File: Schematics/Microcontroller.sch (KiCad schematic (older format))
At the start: 26 parts, among them CON1 USB-MICRO-B, IC1 ATXMEGA256A3BU-A, J1 AVR_JTAG_Header, P1 CONN_02X08, SW1 SW_PUSH, SW2 SW_PUSH, SW3 SW_PUSH, SW4 SW_PUSH, X1 12MHz, X2 32.768KhZ

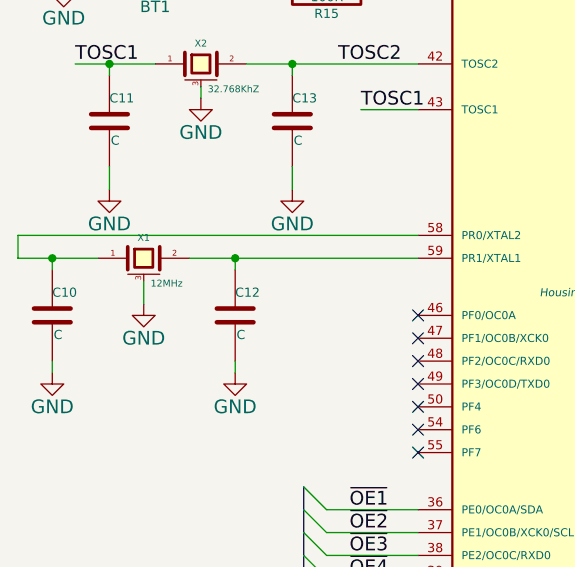
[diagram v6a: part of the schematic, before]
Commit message: Changed lots
Finalised the Inductor. Closes #5
Changed USB Connector. Closes #4
Added four switches for a simple interface. Closes #7
Added a power jack. Closes #3
Found RTC Oscillator. Closes #1.
Added part numbers to all major components. Closes #2
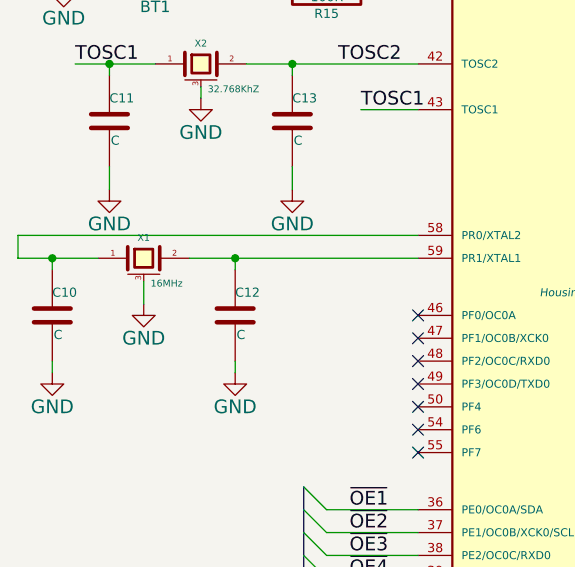
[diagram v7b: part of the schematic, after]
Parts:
- BT1: Part (none) -> BU2032SM-HD-GTR-ND; Supplier (none) -> Digikey
- CON1: footprint usb:USB_Micro-B -> Connect:USB_Mini-B
- IC1: Part (none) -> ATXMEGA256A3BU-A; Supplier (none) -> Farnell
- J1: Part (none) -> FTSH-105-01-L-DV-K-A-P; Supplier (none) -> Farnell
- JP1: footprint SMD_Packages:SMD-0201_r -> Resistors_SMD:R_0603
- P1: footprint (none) -> Socket_Strips:Socket_Strip_Straight_2x08
- SW1, SW2, SW3, SW4: Part (none) -> MC32882; Supplier (none) -> Farnell
- X1: value 12MHz -> 16MHz; Part (none) -> ABM8-16.000MHZ-B2-T; Supplier (none) -> Farnell
- X2: footprint Crystals_Oscillators_SMD:crystal_FA238-TSX3225 -> rgb:SMD_Osc; Part (none) -> ABS06-32.768KHZ-1-T; Supplier (none) -> Farnell
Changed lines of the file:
@@
 F 2 "rgb:FTSH-105-01-L-DV-K-A-P" H 9350 3150 60  0001 C CNN
 F 3 "" H 9350 3150 60  0000 C CNN
+F 4 "FTSH-105-01-L-DV-K-A-P" H 9350 3150 60  0001 C CNN "Part"
+F 5 "Farnell" H 9350 3150 60  0001 C CNN "Supplier"
 	1    9350 3150
 	1    0    0    -1
@@
 SCL
 $Comp
-L VPP #PWR14
+L VPP #PWR03
 U 1 1 54B121F9
 P 9250 1200
-F 0 "#PWR14" H 9250 1050 60  0001 C CNN
+F 0 "#PWR03" H 9250 1050 60  0001 C CNN
 F 1 "VPP" H 9250 1350 60  0000 C CNN
 F 2 "" H 9250 1200 60  0000 C CNN
@@
 $EndComp
 $Comp
-L VPP #PWR10
+L VPP #PWR04
 U 1 1 54B1220F
 P 5800 1450
-F 0 "#PWR10" H 5800 1300 60  0001 C CNN
+F 0 "#PWR04" H 5800 1300 60  0001 C CNN
 F 1 "VPP" H 5800 1600 60  0000 C CNN
 F 2 "" H 5800 1450 60  0000 C CNN
@@
 $EndComp
 $Comp
-L GND #PWR11
+L GND #PWR05
 U 1 1 54B12386
 P 5850 5600
-F 0 "#PWR11" H 5850 5350 60  0001 C CNN
+F 0 "#PWR05" H 5850 5350 60  0001 C CNN
 F 1 "GND" H 5850 5450 60  0000 C CNN
 F 2 "" H 5850 5600 60  0000 C CNN
@@
 TMS
 $Comp
-L VPP #PWR16
+L VPP #PWR06
 U 1 1 54B12F47
 P 9350 2550
-F 0 "#PWR16" H 9350 2400 60  0001 C CNN
+F 0 "#PWR06" H 9350 2400 60  0001 C CNN
 F 1 "VPP" H 9350 2700 60  0000 C CNN
 F 2 "" H 9350 2550 60  0000 C CNN
@@
 $EndComp
 $Comp
-L GND #PWR17
+L GND #PWR07
 U 1 1 54B12FD2
 P 9350 3750
-F 0 "#PWR17" H 9350 3500 60  0001 C CNN
+F 0 "#PWR07" H 9350 3500 60  0001 C CNN
 F 1 "GND" H 9350 3600 60  0000 C CNN
 F 2 "" H 9350 3750 60  0000 C CNN
@@
 TOSC1
 $Comp
-L GND #PWR3
+L GND #PWR08
 U 1 1 54B13B7D
 P 3400 3100
-F 0 "#PWR3" H 3400 2850 60  0001 C CNN
+F 0 "#PWR08" H 3400 2850 60  0001 C CNN
 F 1 "GND" H 3400 2950 60  0000 C CNN
 F 2 "" H 3400 3100 60  0000 C CNN
@@
 $EndComp
 $Comp
-L GND #PWR7
+L GND #PWR09
 U 1 1 54B13BA4
 P 4200 3100
-F 0 "#PWR7" H 4200 2850 60  0001 C CNN
+F 0 "#PWR09" H 4200 2850 60  0001 C CNN
 F 1 "GND" H 4200 2950 60  0000 C CNN
 F 2 "" H 4200 3100 60  0000 C CNN
@@
 $EndComp
 $Comp
-L GND #PWR1
+L GND #PWR010
 U 1 1 54B13F80
 P 3150 3900
-F 0 "#PWR1" H 3150 3650 60  0001 C CNN
+F 0 "#PWR010" H 3150 3650 60  0001 C CNN
 F 1 "GND" H 3150 3750 60  0000 C CNN
 F 2 "" H 3150 3900 60  0000 C CNN
@@
 $EndComp
 $Comp
-L GND #PWR6
+L GND #PWR011
 U 1 1 54B13F86
 P 3950 3900
-F 0 "#PWR6" H 3950 3650 60  0001 C CNN
+F 0 "#PWR011" H 3950 3650 60  0001 C CNN
 F 1 "GND" H 3950 3750 60  0000 C CNN
 F 2 "" H 3950 3900 60  0000 C CNN
@@
 F 0 "CON1" H 9600 5900 50  0000 C CNN
 F 1 "USB-MICRO-B" H 9750 5200 50  0000 C CNN
-F 2 "usb:USB_Micro-B" H 9900 5450 50  0001 C CNN
+F 2 "Connect:USB_Mini-B" H 9900 5450 50  0001 C CNN
 F 3 "" H 9900 5450 50  0000 C CNN
 	1    9900 5550
@@
 $EndComp
 $Comp
-L GND #PWR15
+L GND #PWR012
 U 1 1 54B15BE6
 P 9250 5850
-F 0 "#PWR15" H 9250 5600 60  0001 C CNN
+F 0 "#PWR012" H 9250 5600 60  0001 C CNN
 F 1 "GND" H 9250 5700 60  0000 C CNN
 F 2 "" H 9250 5850 60  0000 C CNN
@@
 $EndComp
 $Comp
-L GND #PWR19
+L GND #PWR013
 U 1 1 54B15BFC
 P 10450 5850
-F 0 "#PWR19" H 10450 5600 60  0001 C CNN
+F 0 "#PWR013" H 10450 5600 60  0001 C CNN
 F 1 "GND" H 10450 5700 60  0000 C CNN
 F 2 "" H 10450 5850 60  0000 C CNN
@@
 F 1 "3V" H 3600 1910 50  0000 C CNN
 F 2 "rgb:BU2032SM-HD-GTR-ND" H 3600 2100 60  0001 C CNN
-F 3 "" H 3600 2100 60  0000 C CNN
+F 3 "http://www.memoryprotectiondevices.com/datasheets/BU2032SM-HD-G-datasheet.pdf" H 3600 2100 60  0001 C CNN
+F 4 "BU2032SM-HD-GTR-ND" H 3600 2100 60  0001 C CNN "Part"
+F 5 "Digikey" H 3600 2100 60  0001 C CNN "Supplier"
 	1    3600 2100
 	-1   0    0    1
@@
 $EndComp
 $Comp
-L GND #PWR2
+L GND #PWR014
 U 1 1 54B17721
 P 3200 2200
-F 0 "#PWR2" H 3200 1950 60  0001 C CNN
+F 0 "#PWR014" H 3200 1950 60  0001 C CNN
 F 1 "GND" H 3200 2050 60  0000 C CNN
 F 2 "" H 3200 2200 60  0000 C CNN
@@
 $EndComp
 $Comp
-L VPP #PWR9
+L VPP #PWR015
 U 1 1 54B284BD
 P 4900 900
-F 0 "#PWR9" H 4900 750 60  0001 C CNN
+F 0 "#PWR015" H 4900 750 60  0001 C CNN
 F 1 "VPP" H 4900 1050 60  0000 C CNN
 F 2 "" H 4900 900 60  0000 C CNN
@@
 $EndComp
 $Comp
-L GND #PWR8
+L GND #PWR016
 U 1 1 54B28C09
 P 4250 1600
-F 0 "#PWR8" H 4250 1350 60  0001 C CNN
+F 0 "#PWR016" H 4250 1350 60  0001 C CNN
 F 1 "GND" H 4250 1450 60  0000 C CNN
 F 2 "" H 4250 1600 60  0000 C CNN
@@
 F 0 "X2" H 3800 2640 30  0000 C CNN
 F 1 "32.768KhZ" H 3830 2440 30  0000 L CNN
-F 2 "Crystals_Oscillators_SMD:crystal_FA238-TSX3225" H 3800 2550 60  0001 C CNN
-F 3 "" H 3800 2550 60  0000 C CNN
+F 2 "rgb:SMD_Osc" H 3800 2550 60  0001 C CNN
+F 3 "http://www.abracon.com/Resonators/ABS06.pdf" H 3800 2550 60  0001 C CNN
+F 4 "ABS06-32.768KHZ-1-T" H 3800 2550 60  0001 C CNN "Part"
+F 5 "Farnell" H 3800 2550 60  0001 C CNN "Supplier"
 	1    3800 2550
 	1    0    0    -1
 $EndComp
 $Comp
-L GND #PWR5
+L GND #PWR017
 U 1 1 54B26812
 P 3800 2700
-F 0 "#PWR5" H 3800 2450 60  0001 C CNN
+F 0 "#PWR017" H 3800 2450 60  0001 C CNN
 F 1 "GND" H 3800 2550 60  0000 C CNN
 F 2 "" H 3800 2700 60  0000 C CNN
@@
 P 3550 3400
 F 0 "X1" H 3550 3490 30  0000 C CNN
-F 1 "12MHz" H 3580 3290 30  0000 L CNN
+F 1 "16MHz" H 3580 3290 30  0000 L CNN
 F 2 "Crystals_Oscillators_SMD:crystal_FA238-TSX3225" H 3550 3400 60  0001 C CNN
-F 3 "" H 3550 3400 60  0000 C CNN
+F 3 "http://www.farnell.com/datasheets/97450.pdf" H 3550 3400 60  0001 C CNN
+F 4 "ABM8-16.000MHZ-B2-T" H 3550 3400 60  0001 C CNN "Part"
+F 5 "Farnell" H 3550 3400 60  0001 C CNN "Supplier"
 	1    3550 3400
 	1    0    0    -1
 $EndComp
 $Comp
-L GND #PWR4
+L GND #PWR018
 U 1 1 54B26B40
 P 3550 3600
-F 0 "#PWR4" H 3550 3350 60  0001 C CNN
+F 0 "#PWR018" H 3550 3350 60  0001 C CNN
 F 1 "GND" H 3550 3450 60  0000 C CNN
 F 2 "" H 3550 3600 60  0000 C CNN
@@
 F 0 "JP1" H 10200 2600 60  0000 C CNN
 F 1 "JUMPER" H 10200 2370 40  0000 C CNN
-F 2 "SMD_Packages:SMD-0201_r" H 10200 2450 60  0001 C CNN
+F 2 "Resistors_SMD:R_0603" H 10200 2450 60  0001 C CNN
 F 3 "" H 10200 2450 60  0000 C CNN
 	1    10200 2450
@@
 $EndComp
 $Comp
-L GND #PWR20
+L GND #PWR019
 U 1 1 54B2A340
 P 10550 2550
-F 0 "#PWR20" H 10550 2300 60  0001 C CNN
+F 0 "#PWR019" H 10550 2300 60  0001 C CNN
 F 1 "GND" H 10550 2400 60  0000 C CNN
 F 2 "" H 10550 2550 60  0000 C CNN
@@
 $EndComp
 $Comp
-L VPP #PWR18
+L VPP #PWR020
 U 1 1 54B2B24F
 P 9850 1850
-F 0 "#PWR18" H 9850 1700 60  0001 C CNN
+F 0 "#PWR020" H 9850 1700 60  0001 C CNN
 F 1 "VPP" H 9850 2000 60  0000 C CNN
 F 2 "" H 9850 1850 60  0000 C CNN
@@
 F 2 "Housings_QFP:TQFP-64_14x14mm_Pitch0.8mm" H 5850 3550 35  0000 C CIN
 F 3 "" H 5850 3550 60  0000 C CNN
+F 4 "ATXMEGA256A3BU-A" H 5850 3550 60  0001 C CNN "Part"
+F 5 "Farnell" H 5850 3550 60  0001 C CNN "Supplier"
 	1    5850 3550
 	1    0    0    -1
@@
 F 0 "P1" H 8550 4450 50  0000 C CNN
 F 1 "CONN_02X08" V 8550 4000 50  0000 C CNN
-F 2 "" H 8550 2800 60  0000 C CNN
+F 2 "Socket_Strips:Socket_Strip_Straight_2x08" H 8550 2800 60  0001 C CNN
 F 3 "" H 8550 2800 60  0000 C CNN
 	1    8550 4000
@@
 $EndComp
 $Comp
-L GND #PWR13
+L GND #PWR021
 U 1 1 54C80C62
 P 8900 4450
-F 0 "#PWR13" H 8900 4200 60  0001 C CNN
+F 0 "#PWR021" H 8900 4200 60  0001 C CNN
 F 1 "GND" H 8900 4300 60  0000 C CNN
 F 2 "" H 8900 4450 60  0000 C CNN
@@
 F 0 "SW1" H 7900 1460 50  0000 C CNN
 F 1 "SW_PUSH" H 7750 1270 50  0000 C CNN
-F 2 "" H 7750 1350 60  0000 C CNN
-F 3 "" H 7750 1350 60  0000 C CNN
+F 2 "" H 7750 1350 60  0001 C CNN
+F 3 "http://www.newark.com/pdfs/datasheets/spc/Ta-1143.pdf" H 7750 1350 60  0001 C CNN
+F 4 "MC32882" H 7750 1350 60  0001 C CNN "Part"
+F 5 "Farnell" H 7750 1350 60  0001 C CNN "Supplier"
 	1    7750 1350
-	1    0    0    -1
-$EndComp
-$Comp
-L SW_PUSH SW2
-U 1 1 54C971DE
-P 7750 1650
-F 0 "SW2" H 7900 1760 50  0000 C CNN
-F 1 "SW_PUSH" H 7750 1570 50  0000 C CNN
-F 2 "" H 7750 1650 60  0000 C CNN
-F 3 "" H 7750 1650 60  0000 C CNN
-	1    7750 1650
-	1    0    0    -1
-$EndComp
-$Comp
-L SW_PUSH SW3
-U 1 1 54C9721C
-P 7750 1950
-F 0 "SW3" H 7900 2060 50  0000 C CNN
-F 1 "SW_PUSH" H 7750 1870 50  0000 C CNN
-F 2 "" H 7750 1950 60  0000 C CNN
-F 3 "" H 7750 1950 60  0000 C CNN
-	1    7750 1950
-	1    0    0    -1
-$EndComp
-$Comp
-L SW_PUSH SW4
-U 1 1 54C97263
-P 7750 2250
-F 0 "SW4" H 7900 2360 50  0000 C CNN
-F 1 "SW_PUSH" H 7750 2170 50  0000 C CNN
-F 2 "" H 7750 2250 60  0000 C CNN
-F 3 "" H 7750 2250 60  0000 C CNN
-	1    7750 2250
 	1    0    0    -1
 $EndComp
@@
 Connection ~ 8150 1650
 $Comp
-L GND #PWR12
+L GND #PWR022
 U 1 1 54C97F8A
 P 8150 2400
-F 0 "#PWR12" H 8150 2150 60  0001 C CNN
+F 0 "#PWR022" H 8150 2150 60  0001 C CNN
 F 1 "GND" H 8150 2250 60  0000 C CNN
 F 2 "" H 8150 2400 60  0000 C CNN
@@
 	1    0    0    -1
 $EndComp
+$Comp
+L SW_PUSH SW2
+U 1 1 54C9B3E4
+P 7750 1650
+F 0 "SW2" H 7900 1760 50  0000 C CNN
+F 1 "SW_PUSH" H 7750 1570 50  0000 C CNN
+F 2 "" H 7750 1650 60  0001 C CNN
+F 3 "http://www.newark.com/pdfs/datasheets/spc/Ta-1143.pdf" H 7750 1650 60  0001 C CNN
+F 4 "MC32882" H 7750 1650 60  0001 C CNN "Part"
+F 5 "Farnell" H 7750 1650 60  0001 C CNN "Supplier"
+	1    7750 1650
+	1    0    0    -1
+$EndComp
+$Comp
+L SW_PUSH SW3
+U 1 1 54C9B54A
+P 7750 1950
+F 0 "SW3" H 7900 2060 50  0000 C CNN
+F 1 "SW_PUSH" H 7750 1870 50  0000 C CNN
+F 2 "" H 7750 1950 60  0001 C CNN
+F 3 "http://www.newark.com/pdfs/datasheets/spc/Ta-1143.pdf" H 7750 1950 60  0001 C CNN
+F 4 "MC32882" H 7750 1950 60  0001 C CNN "Part"
+F 5 "Farnell" H 7750 1950 60  0001 C CNN "Supplier"
+	1    7750 1950
+	1    0    0    -1
+$EndComp
+$Comp
+L SW_PUSH SW4
+U 1 1 54C9B587
+P 7750 2250
+F 0 "SW4" H 7900 2360 50  0000 C CNN
+F 1 "SW_PUSH" H 7750 2170 50  0000 C CNN
+F 2 "" H 7750 2250 60  0001 C CNN
+F 3 "http://www.newark.com/pdfs/datasheets/spc/Ta-1143.pdf" H 7750 2250 60  0001 C CNN
+F 4 "MC32882" H 7750 2250 60  0001 C CNN "Part"
+F 5 "Farnell" H 7750 2250 60  0001 C CNN "Supplier"
+	1    7750 2250
+	1    0    0    -1
+$EndComp

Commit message: Ammended a net. Done a lot of routing
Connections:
- net labels added: JUMPER
- wire segments 138 -> 139
- no-connect marks 17 -> 16
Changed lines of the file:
@@
 NoConn ~ 6950 2550
 NoConn ~ 6950 2450
-NoConn ~ 6950 2350
 $Comp
 L CONN_02X08 P1
@@
 	9850 1900 9850 1850
 Wire Wire Line
-	9700 2450 9900 2450
+	9500 2450 9900 2450
 Wire Wire Line
 	9850 2400 9850 2450
@@
 	1    0    0    -1
 $EndComp
+Wire Wire Line
+	6950 2350 7250 2350
+Text Label 9500 2450 0    60   ~ 0
+JUMPER
+Text Label 7100 2350 0    60   ~ 0
+JUMPER
 $EndSCHEMATC
